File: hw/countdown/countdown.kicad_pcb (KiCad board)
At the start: 4 copper layers, 44 x 23 mm, 24 parts, among them J1 TC2030-SWD, SW1 TS-1187A-B-A-B, U1 STM32L031G6U6, Y1 32.768kHz

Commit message: Prompt log: footprint review; fab export zips gerbers
Co-Authored-By: Claude Fable 5 <noreply@anthropic.com>
Claude-Session: https://claude.ai/code/session_01EyK7WVGPpPEnSjWLWWV8on
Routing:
- net GND: track 19.6 -> 150.7 mm
- net VDD: track 21.4 -> 134.8 mm
- net SEG_DP: track 0.00 -> 78.9 mm, vias 0 -> 2
- net SEG_G: track 0.00 -> 76.6 mm, vias 0 -> 1
- net SEG_E: track 0.00 -> 53.2 mm, vias 0 -> 3
- net DIG_1: track 0.00 -> 51.1 mm, vias 0 -> 1
- net SEG_A: track 0.00 -> 48.1 mm, vias 0 -> 1
- net BOOT0: track 0.00 -> 46.4 mm, vias 0 -> 2
- net DIG_2: track 0.00 -> 38.3 mm, vias 0 -> 1
- net SEG_C: track 0.00 -> 35.7 mm, vias 0 -> 2
- net NRST: track 0.00 -> 30.4 mm, vias 0 -> 2
- net DIG_4: track 0.00 -> 30.2 mm, vias 0 -> 1
- net SWCLK: track 0.00 -> 24.9 mm
- net SWDIO: track 0.00 -> 24.9 mm
- net SEG_F: track 0.00 -> 24.0 mm, vias 0 -> 2
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- added copper zone on In1.Cu, net GND
- added copper zone on In2.Cu, net VDD
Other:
- board text added: "2026-10-10 12:00"
- board text added: "COUNTDOWN v1 2026"
- board text added: "T-MINUS"

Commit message: Pure-A* routing flow with QFN-first ordering; EP GND pad; edge-track deletion fix
Co-Authored-By: Claude Fable 5 <noreply@anthropic.com>
Claude-Session: https://claude.ai/code/session_01EyK7WVGPpPEnSjWLWWV8on
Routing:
- net GND: track 150.7 -> 21.0 mm, vias 15 -> 16
- net VDD: track 134.8 -> 15.2 mm
- net SEG_E: track 53.2 -> 0.00 mm, vias 3 -> 0
- net SEG_G: track 76.6 -> 23.9 mm, vias 1 -> 2
- net SEG_DP: track 78.9 -> 28.2 mm
- net DIG_4: track 30.2 -> 0.00 mm, vias 1 -> 0
- net SWCLK: track 24.9 -> 0.00 mm
- net NRST: track 30.4 -> 6.08 mm, vias 2 -> 0
- net SEG_A: track 48.1 -> 23.9 mm, vias 1 -> 0
- net DIG_1: track 51.1 -> 27.8 mm, vias 1 -> 2
- net LED_F: track 22.8 -> 0.00 mm
- net SEG_B: track 22.2 -> 0.00 mm, vias 1 -> 0
- net LED_B: track 18.9 -> 0.00 mm, vias 2 -> 0
- net DIG_2: track 38.3 -> 20.3 mm, vias 1 -> 2
- net LED_A: track 14.8 -> 0.00 mm
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
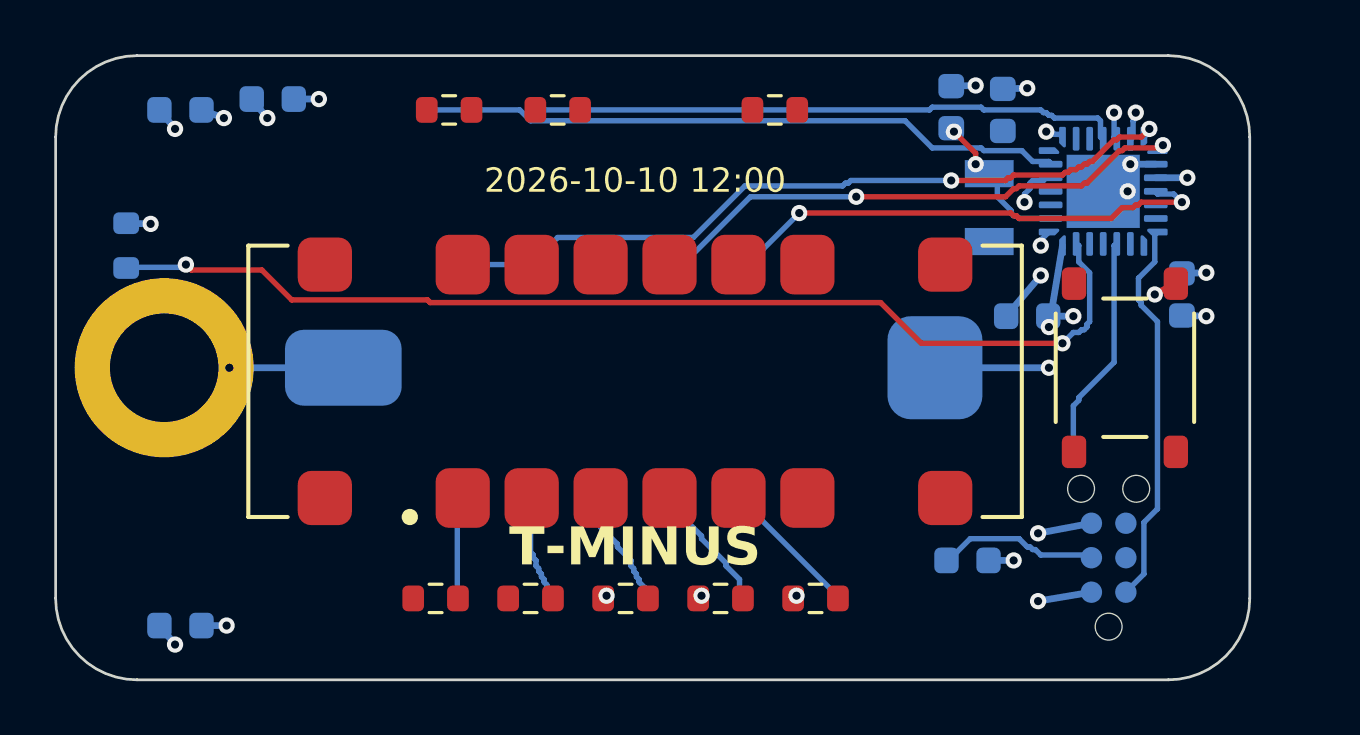
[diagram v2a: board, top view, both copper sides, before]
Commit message: BOARD ROUTED CLEAN: 0 DRC violations, 0 unconnected, 0 parity issues, 0 gate failures (U1 rot90 placement + seed-32 + A* close-out)
Co-Authored-By: Claude Fable 5 <noreply@anthropic.com>
Claude-Session: https://claude.ai/code/session_01EyK7WVGPpPEnSjWLWWV8on
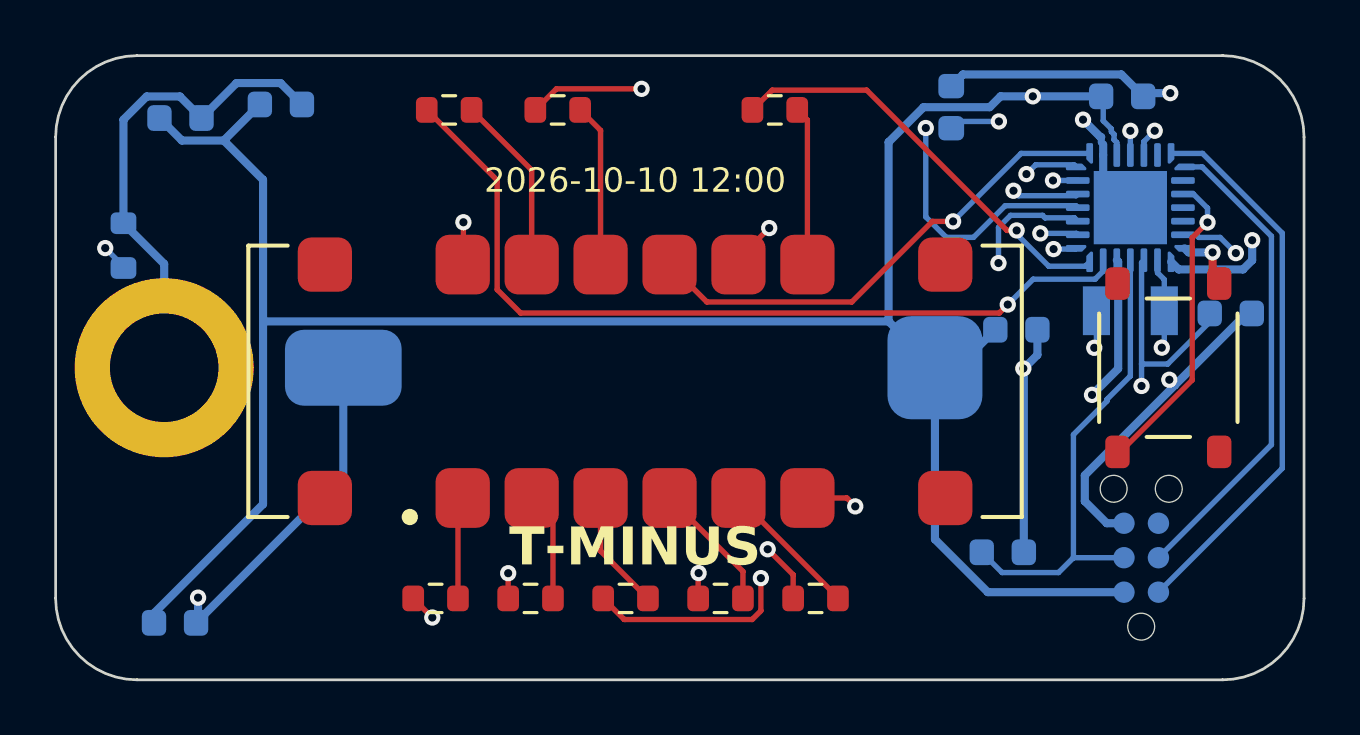
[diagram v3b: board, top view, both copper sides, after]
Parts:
- moved C8 11.3 mm to (43.3, 9.50), turned to 0 degrees
- moved C1 7.62 mm to (39.3, 1.50), turned to 0 degrees
- moved Y1 6.44 mm to (39.6, 9.40), turned to 0 degrees
- moved SW1 1.60 mm to (41.0, 11.5)
- moved C3 1.33 mm to (34.9, 18.3)
- moved J1 1.20 mm to (40.0, 18.5)
- moved U1 1.17 mm to (39.6, 5.60), turned to 90 degrees
- moved C2 0.64 mm to (35.4, 10.1)
- moved C4 0.36 mm to (8.30, 1.80)
- moved C5 0.30 mm to (4.60, 2.30)
- moved C6 0.22 mm to (4.40, 20.9)
- moved R9 0.10 mm to (2.50, 7.00)
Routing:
- net GND: track 21.0 -> 127.5 mm, vias 16 -> 6
- net VDD: track 15.2 -> 117.0 mm, vias 10 -> 3
- net SEG_E: track 0.00 -> 31.8 mm, vias 0 -> 2
- net SEG_D: track 0.00 -> 28.0 mm, vias 0 -> 2
- net DIG_4: track 0.00 -> 21.4 mm, vias 0 -> 2
- net SWCLK: track 0.00 -> 17.8 mm
- net SEG_B: track 0.00 -> 15.6 mm, vias 0 -> 1
- net LSE_IN: track 5.80 -> 20.6 mm
- net LSE_OUT: track 0.00 -> 11.9 mm, vias 0 -> 2
- net NRST: track 6.08 -> 17.6 mm
- net SEG_A: track 23.9 -> 31.4 mm, vias 0 -> 1
- net LED_A: track 0.00 -> 6.62 mm
- net LED_F: track 0.00 -> 6.01 mm
- net SWDIO: track 14.4 -> 20.4 mm
- net LED_B: track 0.00 -> 5.86 mm
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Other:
- board size 44 x 23 mm -> 46 x 23 mm
